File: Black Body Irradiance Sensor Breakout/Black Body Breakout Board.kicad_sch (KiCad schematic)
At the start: 6 parts, among them J1 Conn_01x03, U1 TSL25911FN

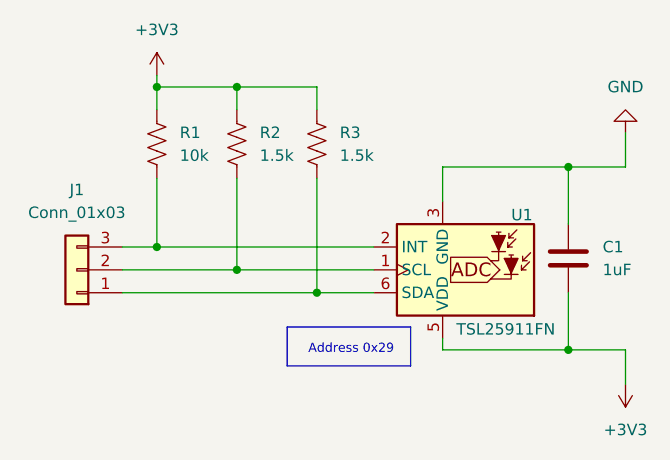
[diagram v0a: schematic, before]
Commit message: arc corners
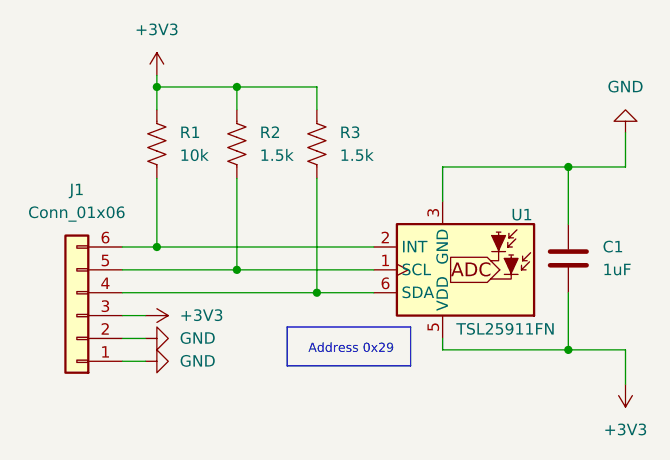
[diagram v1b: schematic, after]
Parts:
- removed J1: Conn_01x03, symbol Connector_Generic:Conn_01x03
- added J1: Conn_01x06, Connector_Molex:Molex_Nano-Fit_105313-xx06_1x06_P2.50mm_Horizontal, symbol Connector_Generic:Conn_01x06
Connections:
- net +3V3: now also J1.3 (Pin_3)
- net GND: now also J1.1 (Pin_1), J1.2 (Pin_2)
- net at R3.2, U1.6 (SDA): now also J1.4 (Pin_4)
- net at R2.2, U1.1 (SCL): now also J1.5 (Pin_5)
- net at R1.2, U1.2 (INT): now also J1.6 (Pin_6)

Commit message: updated connectors
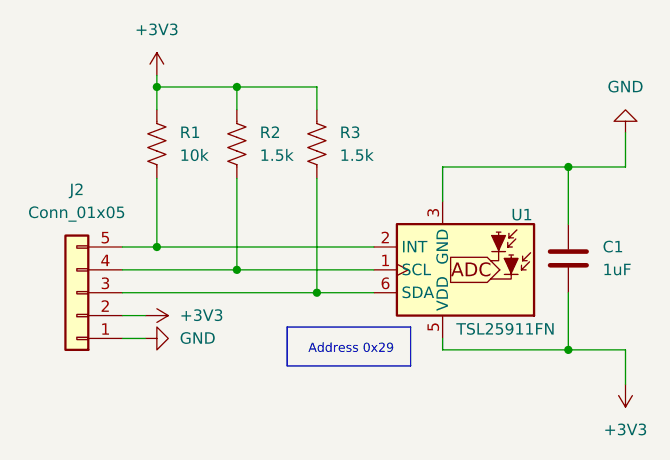
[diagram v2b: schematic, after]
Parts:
- removed J1: Conn_01x06, Connector_Molex:Molex_Nano-Fit_105313-xx06_1x06_P2.50mm_Horizontal, symbol Connector_Generic:Conn_01x06
- added J2: Conn_01x05, Connector_Molex:Molex_Nano-Fit_105313-xx05_1x05_P2.50mm_Horizontal, symbol Connector_Generic:Conn_01x05
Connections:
- net +3V3: now also J2.2 (Pin_2)
- net GND: now also J2.1 (Pin_1)
- net at R3.2, U1.6 (SDA): now also J2.3 (Pin_3)
- net at R2.2, U1.1 (SCL): now also J2.4 (Pin_4)
- net at R1.2, U1.2 (INT): now also J2.5 (Pin_5)
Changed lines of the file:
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@@
 	(wire
 		(pts
-			(xy 93.98 96.52) (xy 96.52 96.52)
+			(xy 93.98 93.98) (xy 96.52 93.98)
 		)
 		(stroke
@@
 	(wire
 		(pts
-			(xy 93.98 93.98) (xy 96.52 93.98)
+			(xy 106.68 76.2) (xy 106.68 86.36)
 		)
 		(stroke
@@
 	(wire
 		(pts
-			(xy 106.68 76.2) (xy 106.68 86.36)
+			(xy 129.54 78.74) (xy 129.54 74.93)
 		)
 		(stroke
@@
 	(wire
 		(pts
-			(xy 129.54 78.74) (xy 129.54 74.93)
+			(xy 129.54 95.25) (xy 143.51 95.25)
 		)
 		(stroke
@@
 		)
 	)
-	(wire
-		(pts
-			(xy 129.54 95.25) (xy 143.51 95.25)
-		)
-		(stroke
-			(width 0)
-			(type default)
-		)
-	)
 	(symbol
 		(lib_id "Device:R_US")
@@
 	)
 	(symbol
+		(lib_id "Connector_Generic:Conn_01x05")
+		(at 88.9 88.9 180)
+		(unit 1)
+		(exclude_from_sim no)
+		(in_bom yes)
+		(on_board yes)
+		(dnp no)
+		(fields_autoplaced yes)
+		(property "Reference" "J2"
+			(at 88.9 77.47 0)
+			(effects
+				(font
+					(size 1.27 1.27)
+				)
+			)
+		)
+		(property "Value" "Conn_01x05"
+			(at 88.9 80.01 0)
+			(effects
+				(font
+					(size 1.27 1.27)
+				)
+			)
+		)
+		(property "Footprint" "Connector_Molex:Molex_Nano-Fit_105313-xx05_1x05_P2.50mm_Horizontal"
+			(at 88.9 88.9 0)
+			(effects
+				(font
+					(size 1.27 1.27)
+				)
+				(hide yes)
+			)
+		)
+		(property "Datasheet" "~"
+			(at 88.9 88.9 0)
+			(effects
+				(font
+					(size 1.27 1.27)
+				)
+				(hide yes)
+			)
+		)
+		(property "Description" "Generic connector, single row, 01x05, script generated (kicad-library-utils/schlib/autogen/connector/)"
+			(at 88.9 88.9 0)
+			(effects
+				(font
+					(size 1.27 1.27)
+				)
+				(hide yes)
+			)
+		)
+		(pin "2"
+		)
+		(pin "1"
+		)
+		(pin "4"
+		)
+		(pin "3"
+		)
+		(pin "5"
+		)
+		(instances
+			(project ""
+				(path "/de4ad0db-6156-4dfe-8fbf-9792d03351ef"
+					(reference "J2")
+					(unit 1)
+				)
+			)
+		)
+	)
+	(symbol
 		(lib_id "power:+3V3")
 		(at 97.79 64.77 0)
@@
 	)
 	(symbol
-		(lib_id "Connector_Generic:Conn_01x06")
-		(at 88.9 91.44 180)
-		(unit 1)
-		(exclude_from_sim no)
-		(in_bom yes)
-		(on_board yes)
-		(dnp no)
-		(fields_autoplaced yes)
-		(property "Reference" "J1"
-			(at 88.9 77.47 0)
-			(effects
-				(font
-					(size 1.27 1.27)
-				)
-			)
-		)
-		(property "Value" "Conn_01x06"
-			(at 88.9 80.01 0)
-			(effects
-				(font
-					(size 1.27 1.27)
-				)
-			)
-		)
-		(property "Footprint" "Connector_Molex:Molex_Nano-Fit_105313-xx06_1x06_P2.50mm_Horizontal"
-			(at 88.9 91.44 0)
-			(effects
-				(font
-					(size 1.27 1.27)
-				)
-				(hide yes)
-			)
-		)
-		(property "Datasheet" "~"
-			(at 88.9 91.44 0)
-			(effects
-				(font
-					(size 1.27 1.27)
-				)
-				(hide yes)
-			)
-		)
-		(property "Description" "Generic connector, single row, 01x06, script generated (kicad-library-utils/schlib/autogen/connector/)"
-			(at 88.9 91.44 0)
-			(effects
-				(font
-					(size 1.27 1.27)
-				)
-				(hide yes)
-			)
-		)
-		(pin "1"
-		)
-		(pin "5"
-		)
-		(pin "2"
-		)
-		(pin "3"
-		)
-		(pin "4"
-		)
-		(pin "6"
-		)
-		(instances
-			(project ""
-				(path "/de4ad0db-6156-4dfe-8fbf-9792d03351ef"
-					(reference "J1")
-					(unit 1)
-				)
-			)
-		)
-	)
-	(symbol
 		(lib_id "Device:R_US")
 		(at 106.68 72.39 0)
@@
 					(unit 1)
 				)
-			)
-		)
-	)
-	(symbol
-		(lib_id "power:GND")
-		(at 96.52 96.52 90)
-		(unit 1)
-		(exclude_from_sim no)
-		(in_bom yes)
-		(on_board yes)
-		(dnp no)
-		(fields_autoplaced yes)
-		(property "Reference" "#PWR06"
-			(at 102.87 96.52 0)
-			(effects
-				(font
-					(size 1.27 1.27)
-				)
-				(hide yes)
-			)
-		)
-		(property "Value" "GND"
-			(at 100.33 96.5199 90)
-			(effects
-				(font
-					(size 1.27 1.27)
-				)
-				(justify right)
-			)
-		)
-		(property "Footprint" ""
-			(at 96.52 96.52 0)
-			(effects
-				(font
-					(size 1.27 1.27)
-				)
-				(hide yes)
-			)
-		)
-		(property "Datasheet" ""
-			(at 96.52 96.52 0)
-			(effects
-				(font
-					(size 1.27 1.27)
-				)
-				(hide yes)
-			)
-		)
-		(property "Description" "Power symbol creates a global label with name \"GND\" , ground"
-			(at 96.52 96.52 0)
-			(effects
-				(font
-					(size 1.27 1.27)
-				)
-				(hide yes)
-			)
-		)
-		(pin "1"
-		)
-		(instances
-			(project "Black Body Breakout Board"
-				(path "/de4ad0db-6156-4dfe-8fbf-9792d03351ef"
-					(reference "#PWR06")
-					(unit 1)
-				)
